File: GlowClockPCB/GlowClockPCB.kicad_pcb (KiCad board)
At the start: 2 copper layers, 115.6 x 67.9 mm, 52 parts, among them J1 LED_OUT_1, J2 LED_OUT_2, J3 LED_OUT_3, J4 LED_OUT_4, J5 POWER_IN, J6 Motor_1_Out, J7 Motor_2_Out, J8 I2C_LCD, J9 ADC_OUT, SW1 BTN_UP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

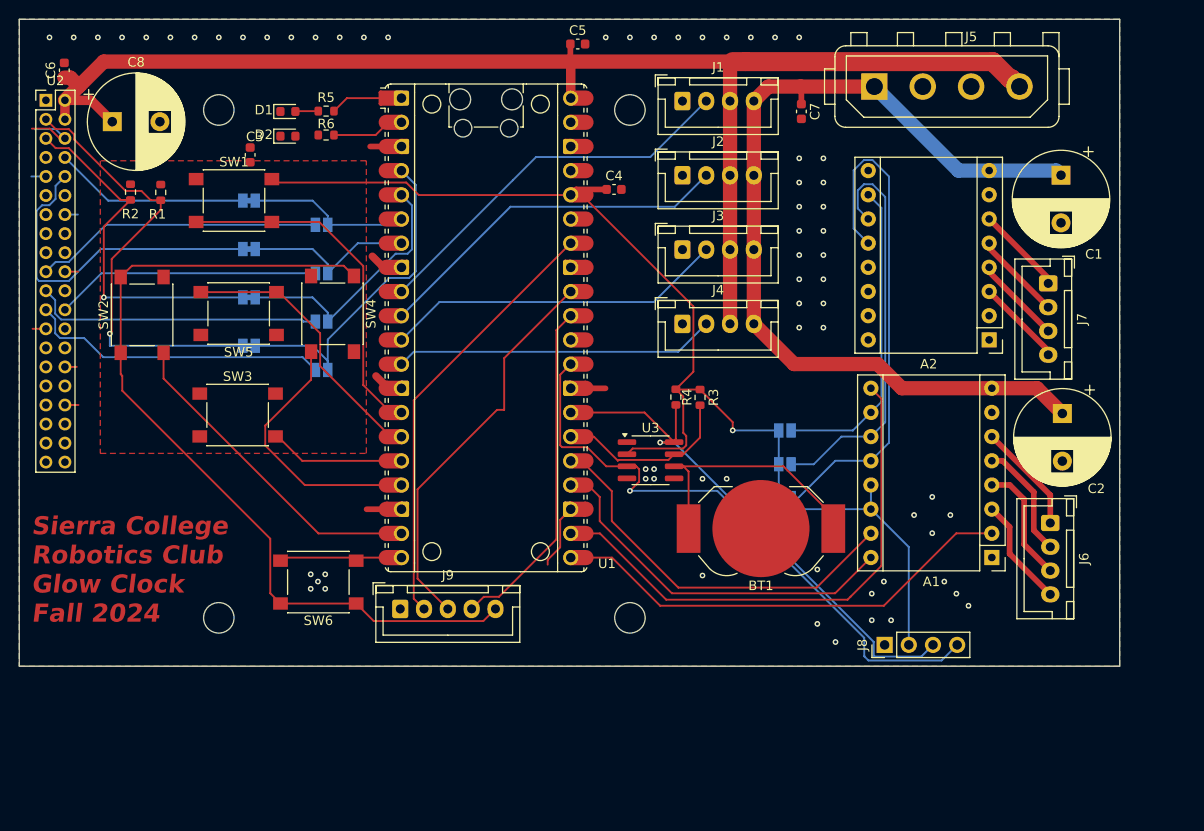
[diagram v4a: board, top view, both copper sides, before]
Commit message: finalize design for export, add schematic to docs
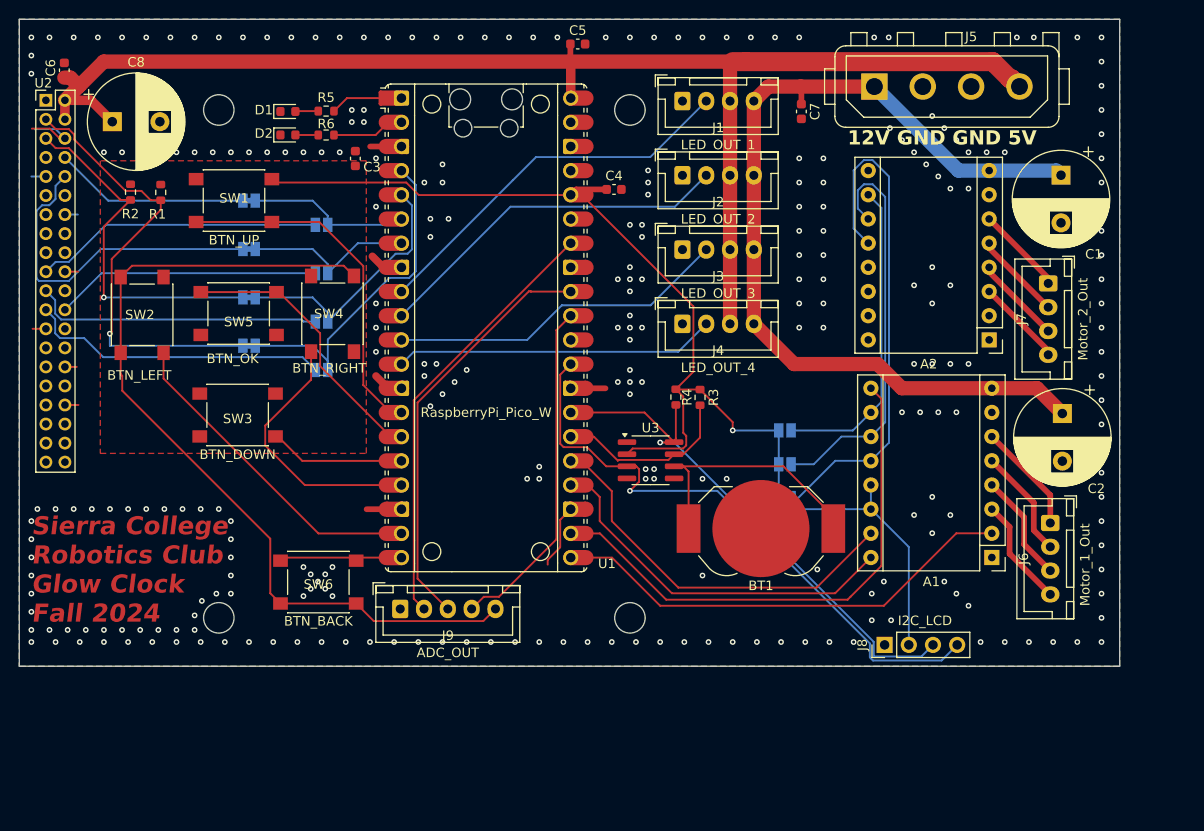
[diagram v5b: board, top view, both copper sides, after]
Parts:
- moved C3 11.1 mm to (90.5, 109.2)
- moved D2 0.13 mm to (83.5, 106.8)
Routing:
- net Net-(D2-A): track 0.00 -> 2.45 mm
- net Net-(J9-Pin_3): track 41.8 -> 43.9 mm
- net Net-(A1-A1): track 12.6 -> 11.5 mm
- net Net-(A1-B1): track 12.2 -> 11.6 mm
- net GND: vias 66 -> 269
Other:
- board text added: "12V GND GND 5V"
- board text added: "PCB Designed by Patrick Leiser V 1.0"
- board text removed: "TODO: DECIDE/CONFIRM OPTIMAL PI ZERO MOUNTING STRATEGY/ORIENTATION; KEEP-OUT ZONE"

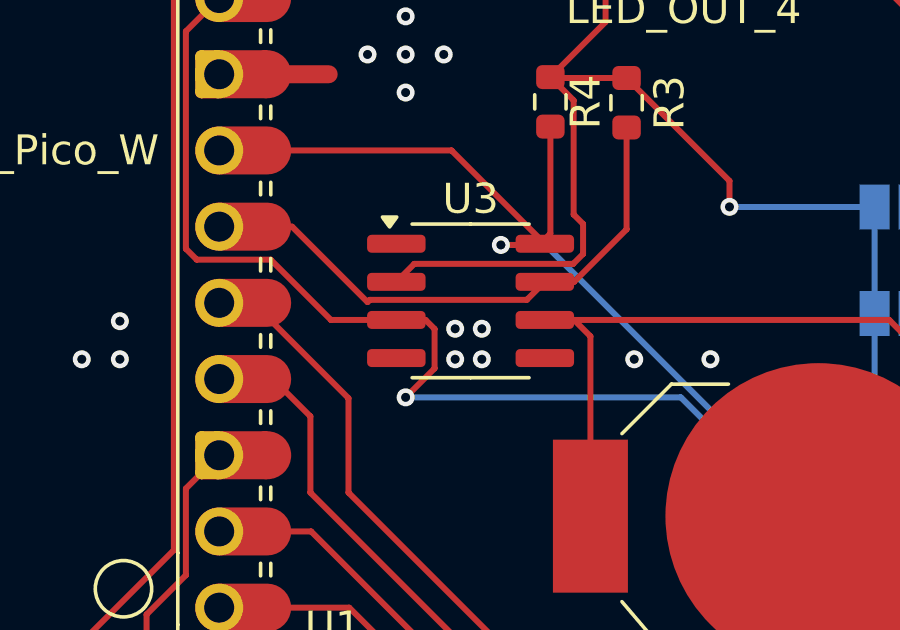
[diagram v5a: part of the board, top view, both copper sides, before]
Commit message: correct SDA connection for I2C_LCD port
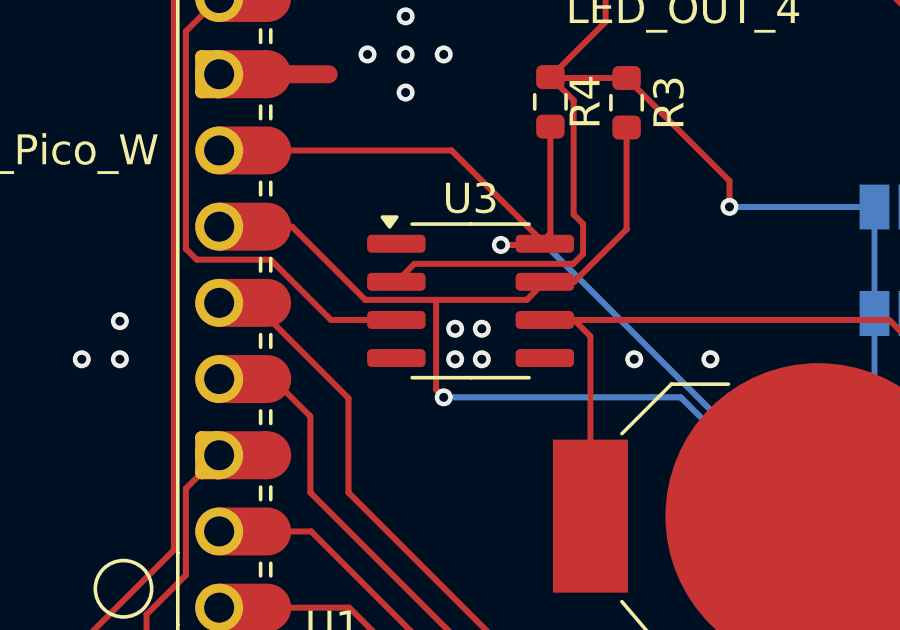
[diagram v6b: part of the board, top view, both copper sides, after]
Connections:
- R3 pad 2: Net-(U1-GPIO20) -> Net-(J8-Pin_4)
- U1 pad 26: Net-(U1-GPIO20) -> Net-(J8-Pin_4)
- U1 pad 29: Net-(J8-Pin_4) -> Net-(U1-GPIO22)
- U3 pad 3: Net-(J8-Pin_4) -> Net-(U1-GPIO22)
- U3 pad 7: Net-(U1-GPIO20) -> Net-(J8-Pin_4)
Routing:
- net Net-(U1-GPIO20): track 19.0 -> 0.00 mm
- net Net-(U1-GPIO22): track 0.00 -> 16.8 mm

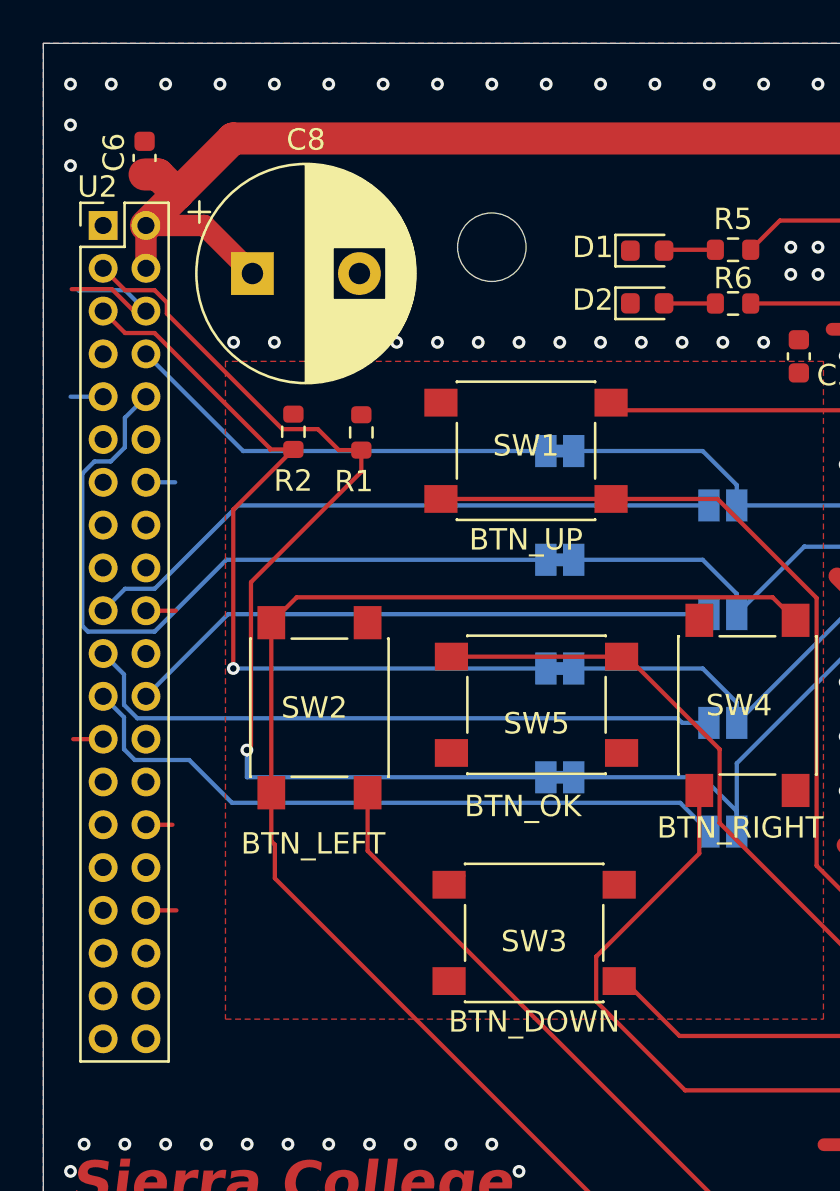
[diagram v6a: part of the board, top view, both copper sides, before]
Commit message: Replace 40 pin 2.0mm header with 26 pin 2.54mm header
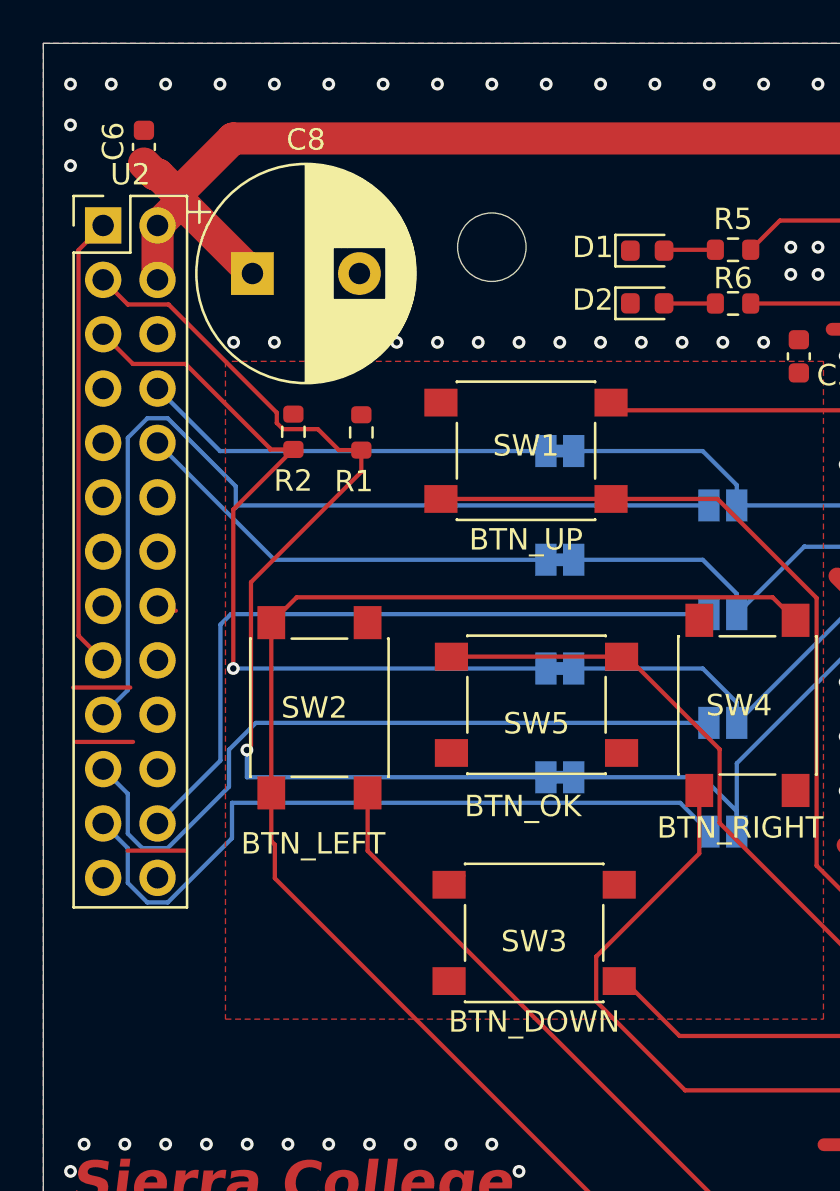
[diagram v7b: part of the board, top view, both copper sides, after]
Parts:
- U2: footprint Connector_PinHeader_2.00mm:PinHeader_2x20_P2.00mm_Vertical -> Connector_PinHeader_2.54mm:PinHeader_2x13_P2.54mm_Vertical
- moved C6 0.51 mm to (59.9, 99.5)
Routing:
- net Net-(U2-3V3-Pad1): track 0.00 -> 21.3 mm
- net Net-(JP2-A): track 35.5 -> 20.4 mm
- net Net-(JP5-A): track 30.3 -> 43.3 mm
- net GND: track 42.1 -> 34.3 mm
- net Net-(JP3-A): track 27.9 -> 34.8 mm
- net Net-(JP4-A): track 30.8 -> 34.7 mm
- net Net-(JP6-A): track 31.8 -> 34.2 mm
- net unconnected-(U2-GPIO23-Pad16): track 0.00 -> 1.40 mm
- net Net-(JP1-A): track 20.6 -> 19.4 mm
- net +5V: track 146.3 -> 145.8 mm

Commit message: pcb updates
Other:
- board text added: "PCB Designed by Patrick Leiser V 1.1"
- board text removed: "PCB Designed by Patrick Leiser V 1.0"
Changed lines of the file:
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@@
 		(tags "connector JST XH vertical")
 		(property "Reference" "J2"
-			(at 3.75 2.8 0)
+			(at 10.868 3.258 0)
 			(layer "F.SilkS")
 			(effects
@@
 		(tags "capacitor")
 		(property "Reference" "C3"
-			(at -0.889 1.745 180)
+			(at -0.616 -1.644 180)
 			(layer "F.SilkS")
 			(effects
@@
 		(tags "connector JST XH vertical")
 		(property "Reference" "J7"
-			(at 3.75 2.8 90)
+			(at -3.483 2.787 180)
 			(layer "F.SilkS")
 			(effects
@@
 		(tags "connector JST XH vertical")
 		(property "Reference" "J4"
-			(at 3.75 2.8 0)
+			(at 11.122 3.131 0)
 			(layer "F.SilkS")
 			(effects
@@
 		(tags "connector JST XH vertical")
 		(property "Reference" "J6"
-			(at 3.75 2.8 90)
+			(at -3.502 2.748 180)
 			(layer "F.SilkS")
 			(effects
@@
 		(tags "connector JST XH vertical")
 		(property "Reference" "J3"
-			(at 3.75 2.8 0)
+			(at 10.868 3.385 0)
 			(layer "F.SilkS")
 			(effects
@@
 		(tags "connector JST XH vertical")
 		(property "Reference" "J1"
-			(at 3.75 2.8 0)
+			(at 10.995 3.131 0)
 			(layer "F.SilkS")
 			(effects
@@
 		(tags "Through hole pin header THT 2x13 2.54mm double row")
 		(property "Reference" "U2"
-			(at 1.27 -2.38 0)
+			(at -0.255 -2.16 0)
 			(layer "F.SilkS")
 			(effects
@@
 		(tags "connector JST XH vertical")
 		(property "Reference" "J9"
-			(at 5 2.8 0)
+			(at 13.711 1.824 0)
 			(layer "F.SilkS")
 			(effects
@@
 		(tags "solder jumper open")
 		(property "Reference" "JP10"
-			(at 3.175 -0.105 0)
+			(at 3.405 0.001 0)
 			(layer "B.SilkS")
 			(effects
@@
 		)
 		(property "Value" "StepperMode1"
-			(at 0 -1.9 0)
+			(at -0.024 -1.777 0)
 			(layer "B.SilkS")
 			(effects
@@
 		(tags "solder jumper open")
 		(property "Reference" "JP11"
-			(at 3.175 -0.105 0)
+			(at 3.278 -0.12 0)
 			(layer "B.SilkS")
 			(effects
@@
 		)
 	)
-	(gr_text "PCB Designed by\nPatrick Leiser\nV 1.0"
+	(gr_text "PCB Designed by\nPatrick Leiser\nV 1.1"
 		(at 76.835 153.67 0)
 		(layer "B.SilkS")
@@
 	)
 	(segment
-		(start 105.622266 155.27)
-		(end 104.03 155.27)
+		(start 111.654969 127.265031)
+		(end 111.654969 149.905931)
 		(width 0.2)
 		(layer "F.Cu")
@@
 	)
 	(segment
-		(start 111.654969 149.237297)
-		(end 105.622266 155.27)
+		(start 106.35 155.2099)
+		(end 104.0901 155.2099)
 		(width 0.2)
 		(layer "F.Cu")
@@
 	)
 	(segment
-		(start 104.03 155.27)
-		(end 102.755 156.545)
+		(start 111.653969 149.905931)
+		(end 106.35 155.2099)
 		(width 0.2)
 		(layer "F.Cu")
@@
 	)
 	(segment
-		(start 111.654969 127.265031)
-		(end 111.654969 149.237297)
+		(start 113.165 125.755)
+		(end 111.654969 127.265031)
 		(width 0.2)
 		(layer "F.Cu")
@@
 	)
 	(segment
-		(start 113.165 125.755)
-		(end 111.654969 127.265031)
+		(start 104.0901 155.2099)
+		(end 102.755 156.545)
 		(width 0.2)
 		(layer "F.Cu")
